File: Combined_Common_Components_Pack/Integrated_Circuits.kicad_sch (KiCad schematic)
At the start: 7 parts, among them U1 ADS1115IDGS, U17 MCP23017_SO

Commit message: Added some connectors and basic parts
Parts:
- added R111: 10k, Resistor_SMD:R_0805_2012Metric, symbol Device:R
- added U22: TXB0102DCU, Package_SO:VSSOP-8_2.3x2mm_P0.5mm, symbol Logic_LevelTranslator:TXB0102DCU
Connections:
- net +3.3V: now also R111.1, U22.3 (VCCA)
- net A1: now also U22.5 (A1)
- net A2: now also U22.4 (A2)
- net GND: now also U22.2 (GND)
- new net +5V: U22.7 (VCCB)
- new net B1: U22.8 (B1)
- new net B2: U22.1 (B2)
- new net SHIFTER_EN: R111.2, U22.6 (OE)

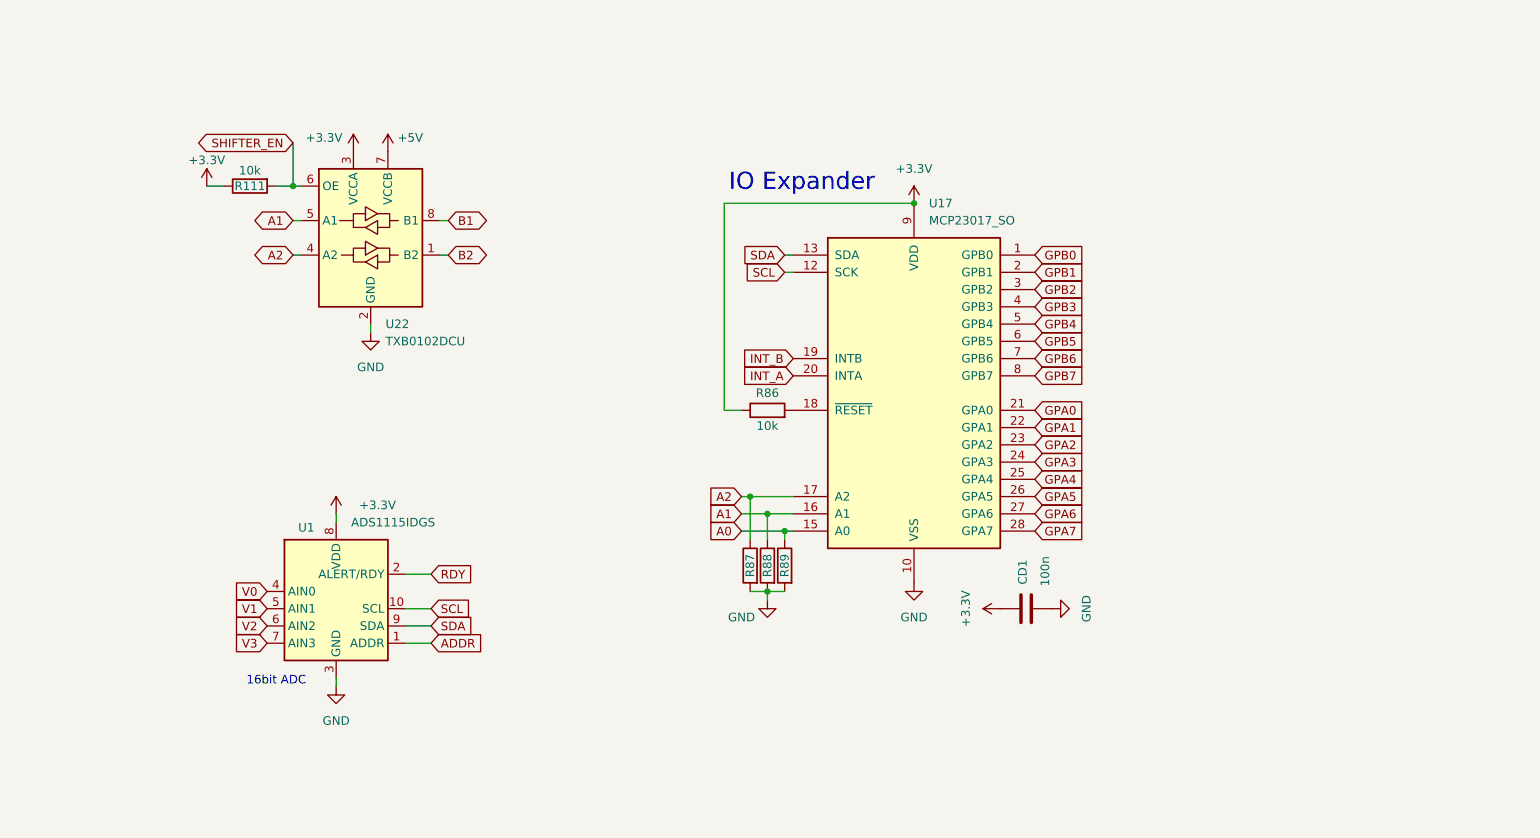
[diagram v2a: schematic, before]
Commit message: Minor updates
Basically components annotation, and more basic parts added
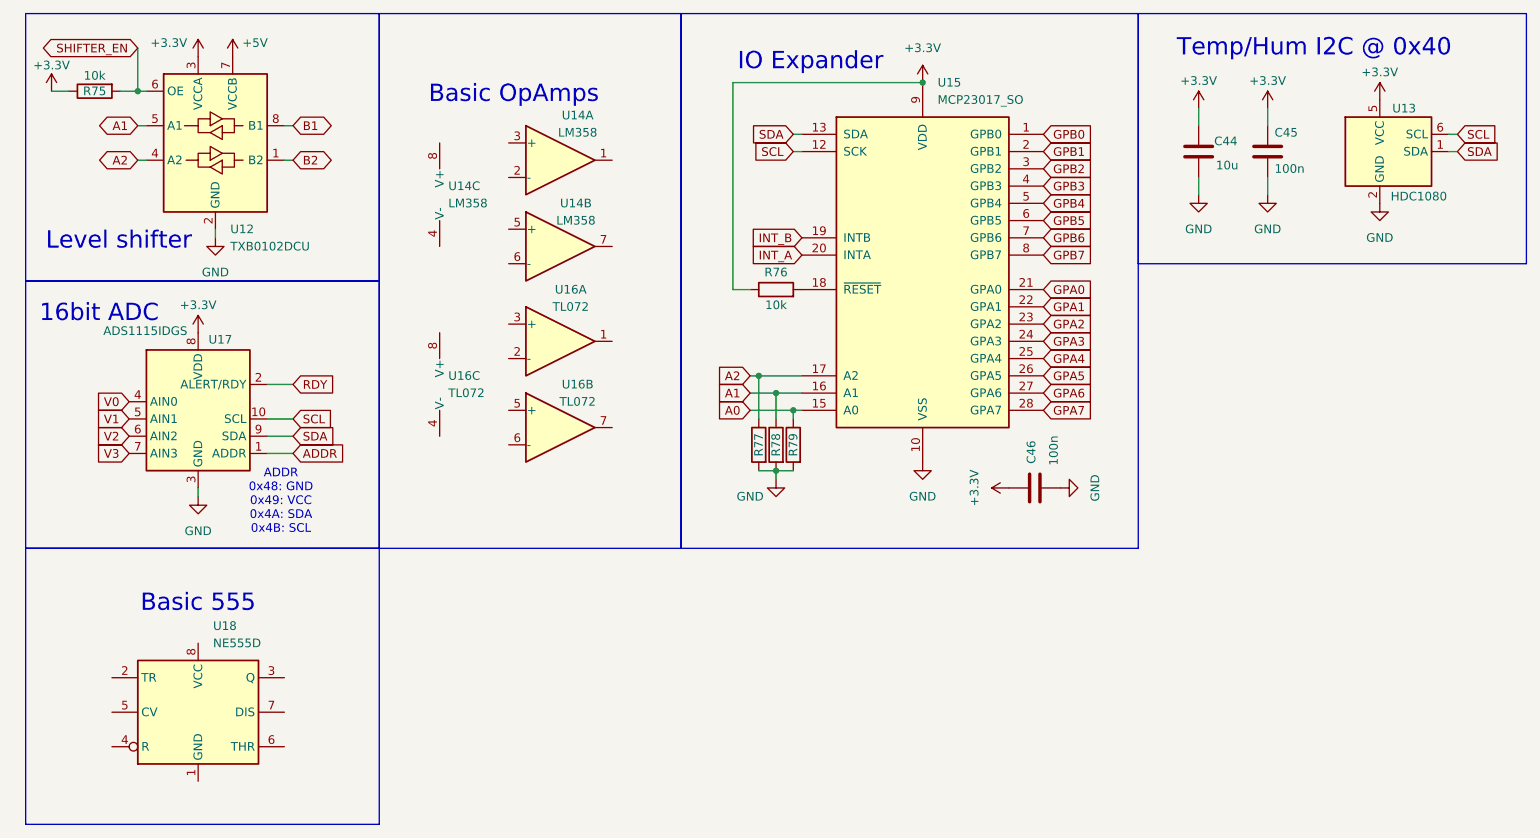
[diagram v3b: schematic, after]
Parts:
- added C44: 10u, Capacitor_SMD:C_0805_2012Metric, symbol Device:C
- added C45: 100n, Capacitor_SMD:C_0402_1005Metric, symbol Device:C
- added U13: HDC1080, Package_SON:Texas_PWSON-N6, symbol Sensor_Humidity:HDC1080
- added U14: LM358, Package_SO:SOIC-8_3.9x4.9mm_P1.27mm, symbol Amplifier_Operational:LM358
- added U16: TL072, Package_SO:SO-8_5.3x6.2mm_P1.27mm, symbol Amplifier_Operational:TL072
- added U18: NE555D, Package_SO:SOIC-8_3.9x4.9mm_P1.27mm, symbol Timer:NE555D
- renumbered CD1 to C46, R111 to R75, R86 to R76, R87 to R77, R88 to R78, R89 to R79, U22 to U12, U17 to U15, U1 to U17
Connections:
- net +3.3V: now also C44.1, C45.1, U13.5 (VCC)
- net GND: now also C44.2, C45.2, U13.2 (GND)
- net SCL: now also U13.6 (SCL)
- net SDA: now also U13.1 (SDA)
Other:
- note added: "ADDR 0x48: GND 0x49: VCC 0x4A: SDA 0x4B: SCL"
- note added: "Basic 555"
- note added: "Basic OpAmps"
- note added: "Level shifter"
- note added: "Temp/Hum I2C @ 0x40"
- moved on the sheet: C46, R75, R76, R77, R78, R79, U12, U15, U17
